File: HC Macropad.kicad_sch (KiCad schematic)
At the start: 31 parts

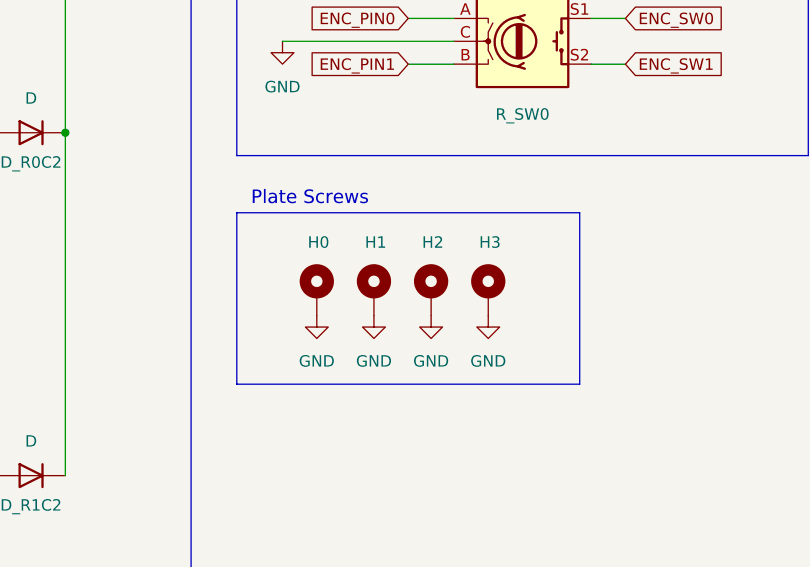
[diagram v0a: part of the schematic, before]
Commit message: Starting to work on the PCB, might need to enlarge it
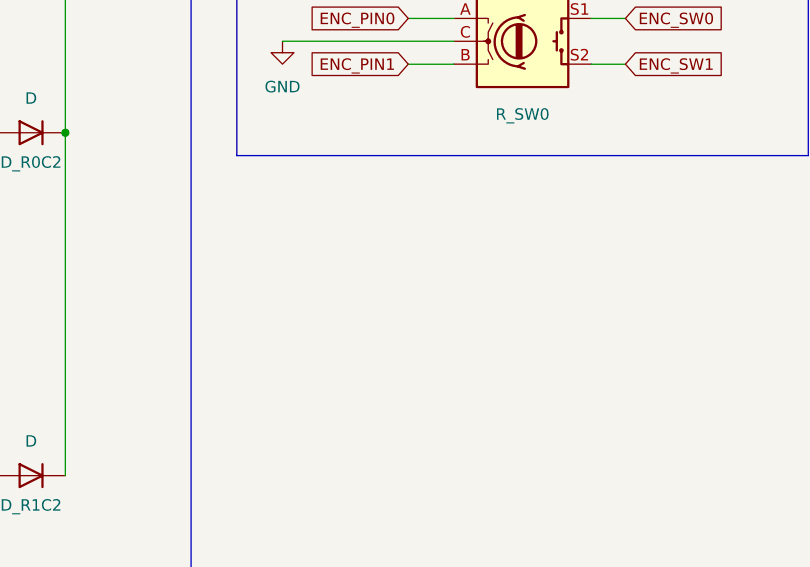
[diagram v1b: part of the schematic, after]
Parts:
- removed H0, H1, H2, H3: MountingHole_Pad, symbol Mechanical:MountingHole_Pad
- SW_R0C0, SW_R0C1, SW_R0C2, SW_R1C0, SW_R1C1, SW_R1C2: footprint (none) -> PCM_marbastlib-mx:SW_MX_1u
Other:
- note removed: "Plate Screws"
